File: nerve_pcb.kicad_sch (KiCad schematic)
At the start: 55 parts, among them J1 TC2050-IDC, J2 2171750001, J4 472192001, J5 BF030-16A-B1-0360-0277-0600-LB, J6 BF080-20-A-1-L-C, J7 UART, SW1 SPST, SW2 SPST, U1 ld39150dt33-r, U2 STM32F446RET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

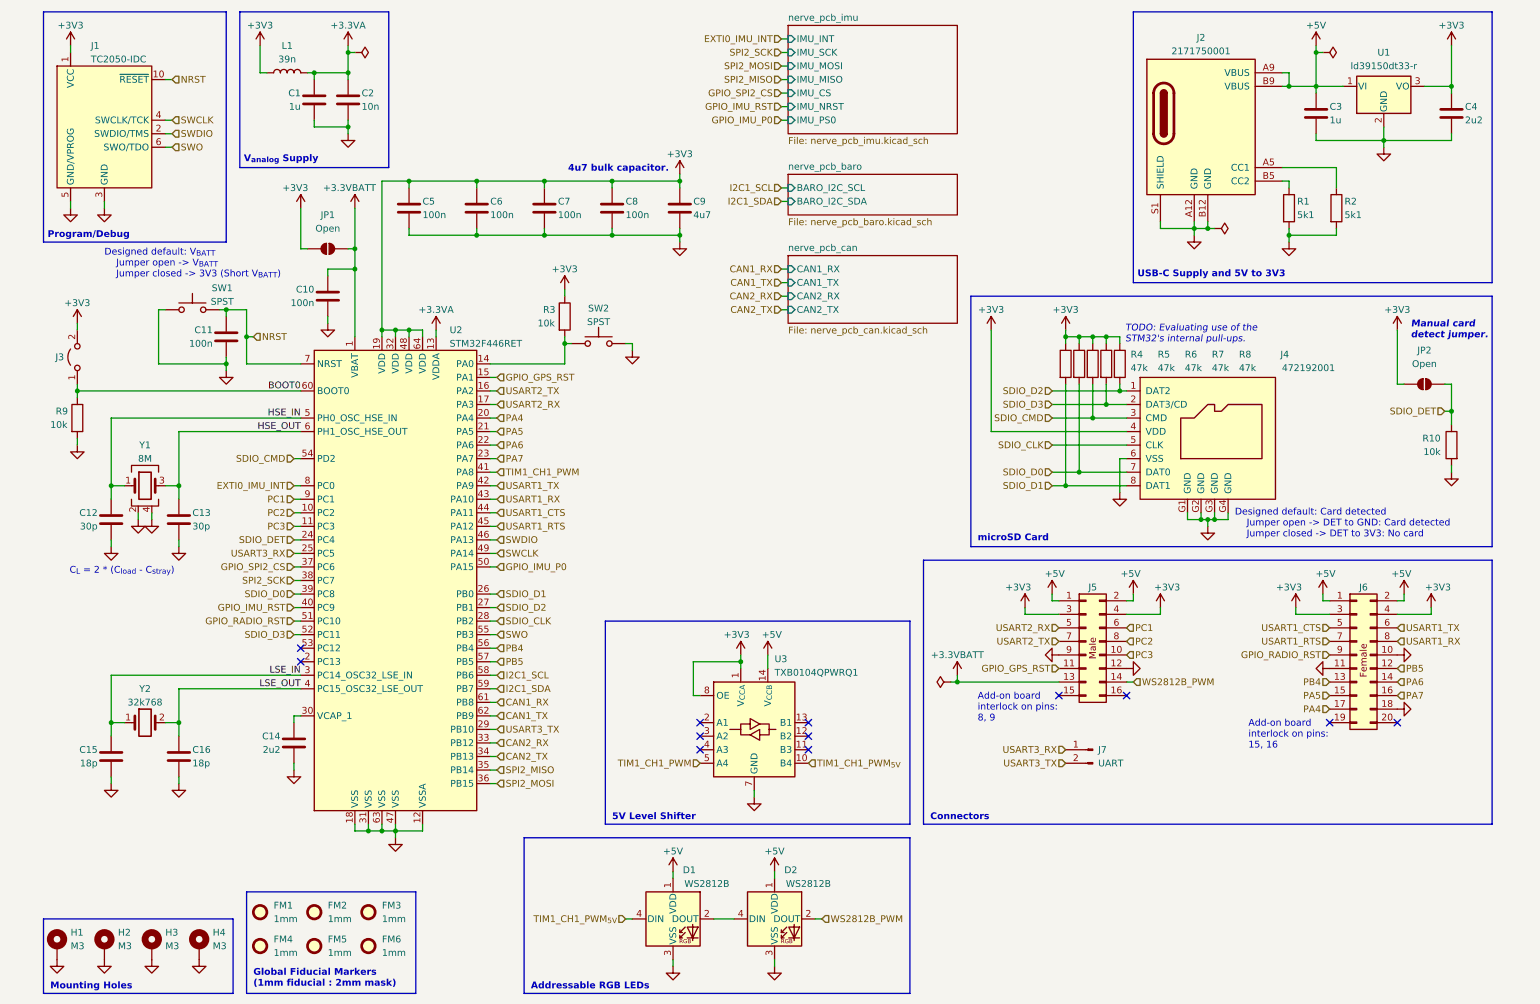
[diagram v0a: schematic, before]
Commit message: Update component_library and cleanup unused pads
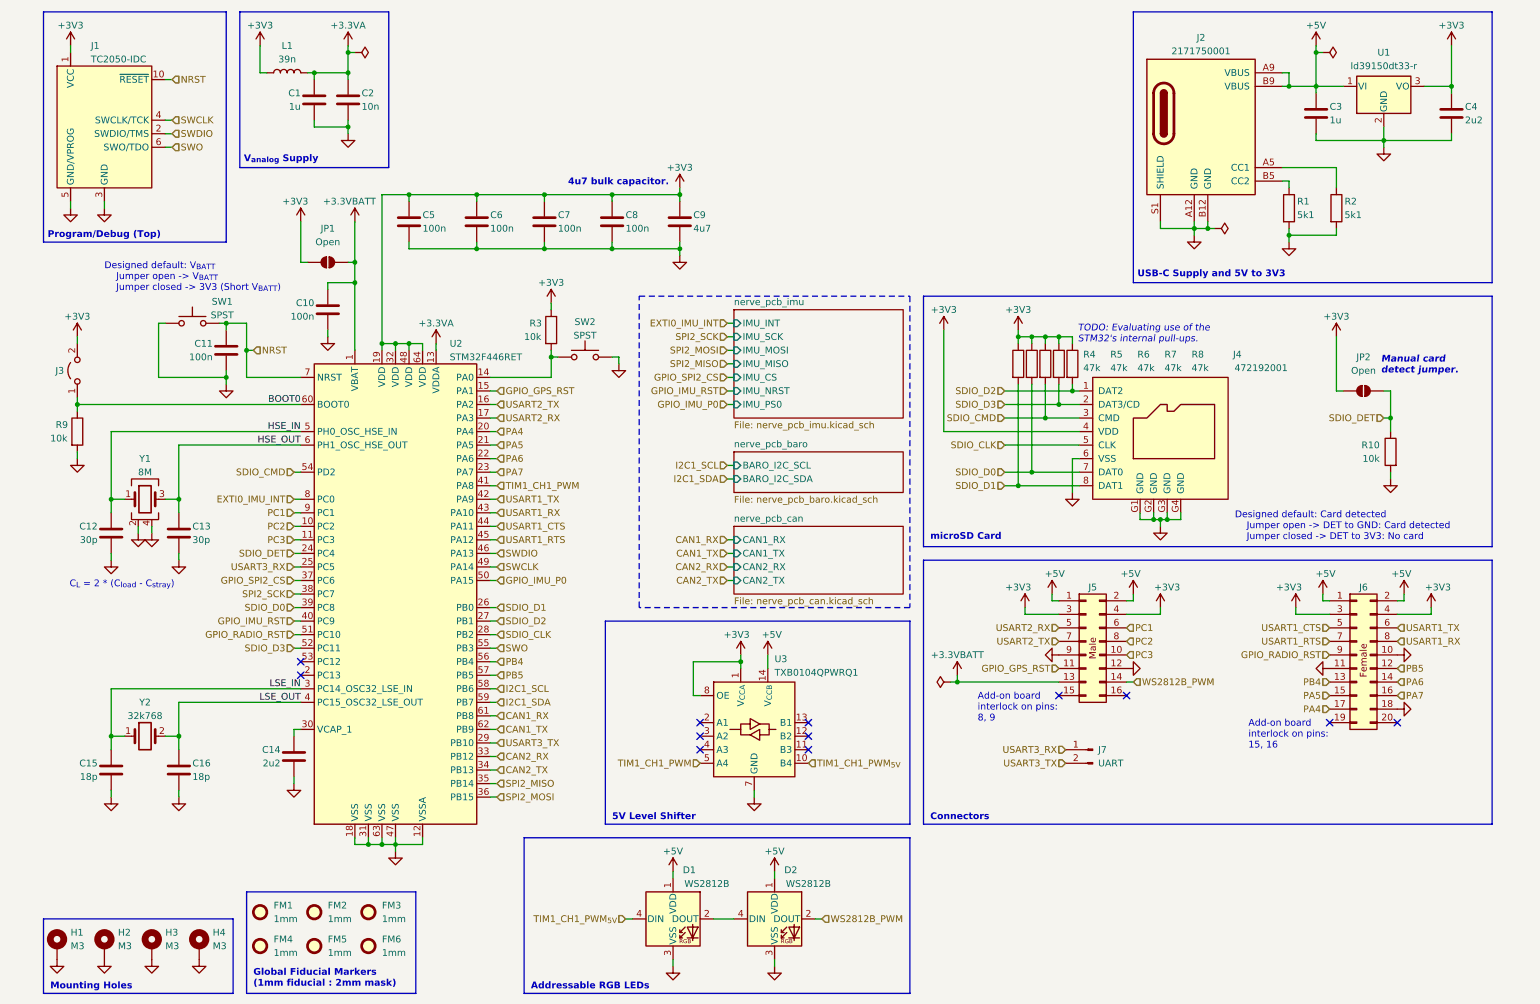
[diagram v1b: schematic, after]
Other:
- note added: "Program/Debug (Top)"
- note removed: "Program/Debug"
- moved on the sheet: C10, C11, C12, C13, C14, C15, C16, C5, C6, C7, C8, C9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

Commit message: Fix schematic notes
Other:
- note added: "4u7 bulk capacitor"
- note added: "Add-on board interlock on pins: 19, 20"
- note added: "Manual card detect jumper"
- note added: "Using external pull-ups"
- note removed: "4u7 bulk capacitor."
- note removed: "Add-on board interlock on pins: 8, 9"
- note removed: "Manual card detect jumper."
- note removed: "TODO: Evaluating use of the STM32's internal pull-ups."
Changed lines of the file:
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@@
 		)
 	)
-	(text "Add-on board\ninterlock on pins:\n8, 9"
+	(text "Add-on board\ninterlock on pins:\n15, 16"
 		(exclude_from_sim no)
 		(at 187.96 143.256 0)
@@
 		)
 	)
-	(text "Add-on board\ninterlock on pins:\n15, 16"
+	(text "Add-on board\ninterlock on pins:\n19, 20"
 		(exclude_from_sim no)
 		(at 238.76 148.336 0)
@@
 		)
 	)
-	(text "Manual card \ndetect jumper."
+	(text "Manual card \ndetect jumper"
 		(exclude_from_sim no)
 		(at 263.652 78.994 0)
@@
 		)
 	)
-	(text "4u7 bulk capacitor."
+	(text "4u7 bulk capacitor"
 		(exclude_from_sim no)
 		(at 130.048 44.704 0)
@@
 		)
 	)
-	(text "TODO: Evaluating use of the \nSTM32's internal pull-ups."
+	(text "Using external pull-ups"
 		(exclude_from_sim no)
-		(at 206.756 73.152 0)
+		(at 208.026 74.168 0)
 		(effects
 			(font
 				(size 1.27 1.27)
-				(thickness 0.1588)
+				(thickness 0.254)
+				(bold yes)
 				(italic yes)
 			)

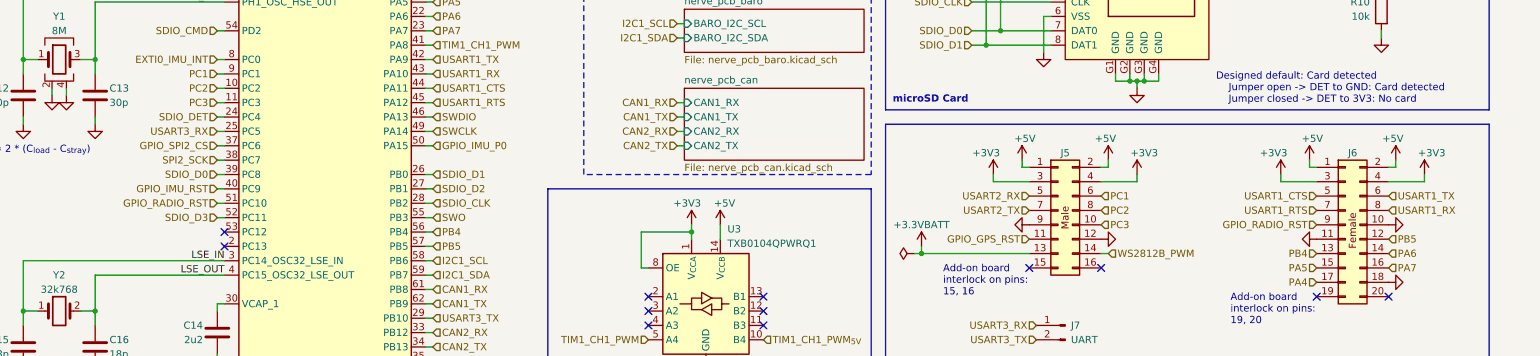
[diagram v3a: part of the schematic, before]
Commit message: Major cleanup and add missing transfer vias
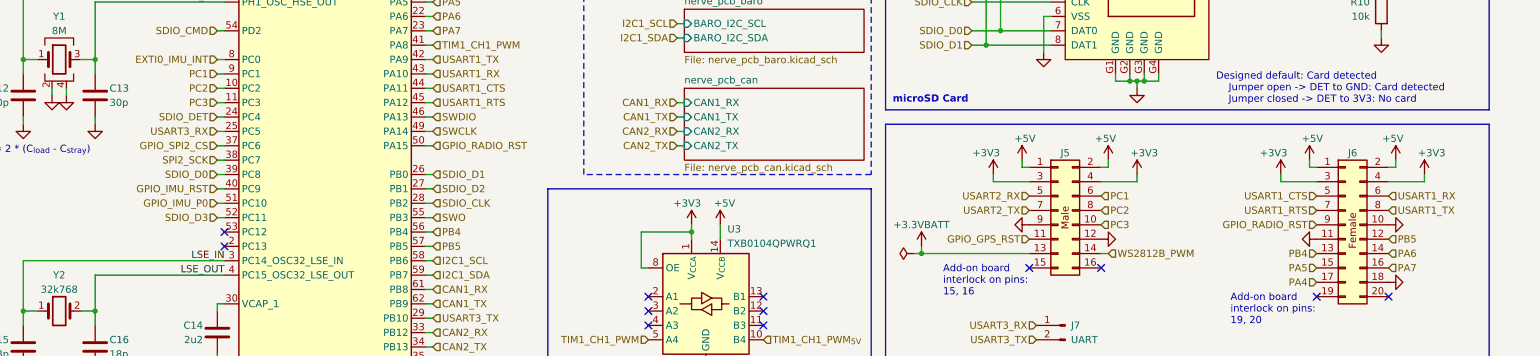
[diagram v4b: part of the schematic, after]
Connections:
- net GPIO_IMU_P0: now also U2.51 (PC10); no longer U2.50 (PA15)
- net GPIO_RADIO_RST: now also U2.50 (PA15); no longer U2.51 (PC10)
- net USART1_RX: now also J6.6; no longer J6.8
- net USART1_TX: now also J6.8; no longer J6.6

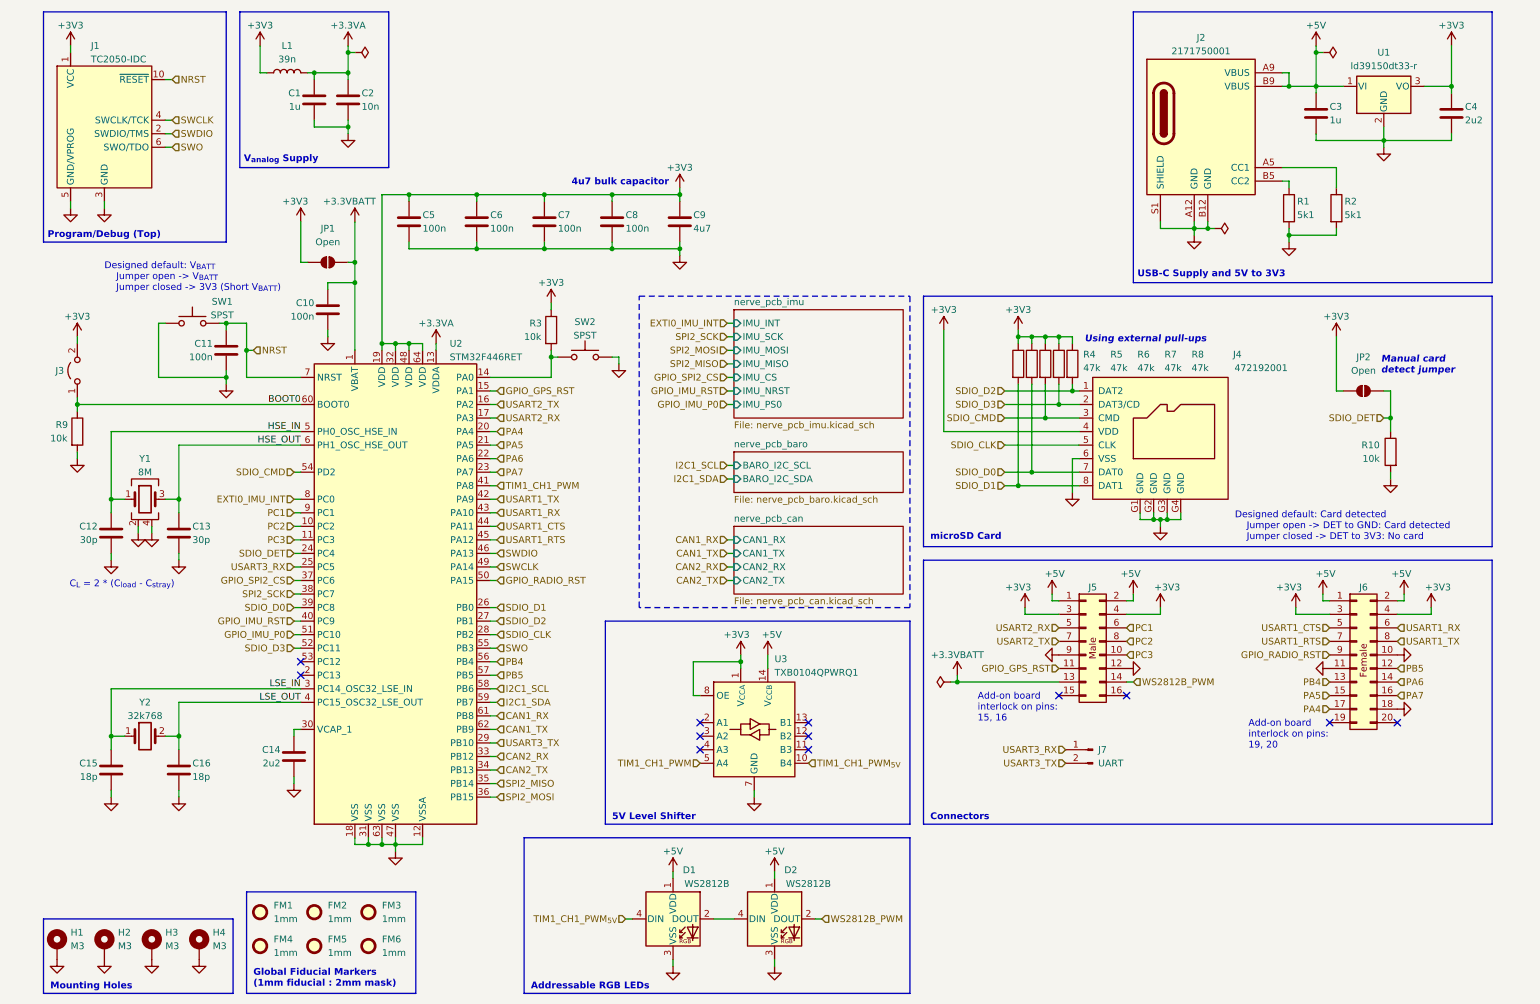
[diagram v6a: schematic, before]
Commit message: Add minor decoupling caps
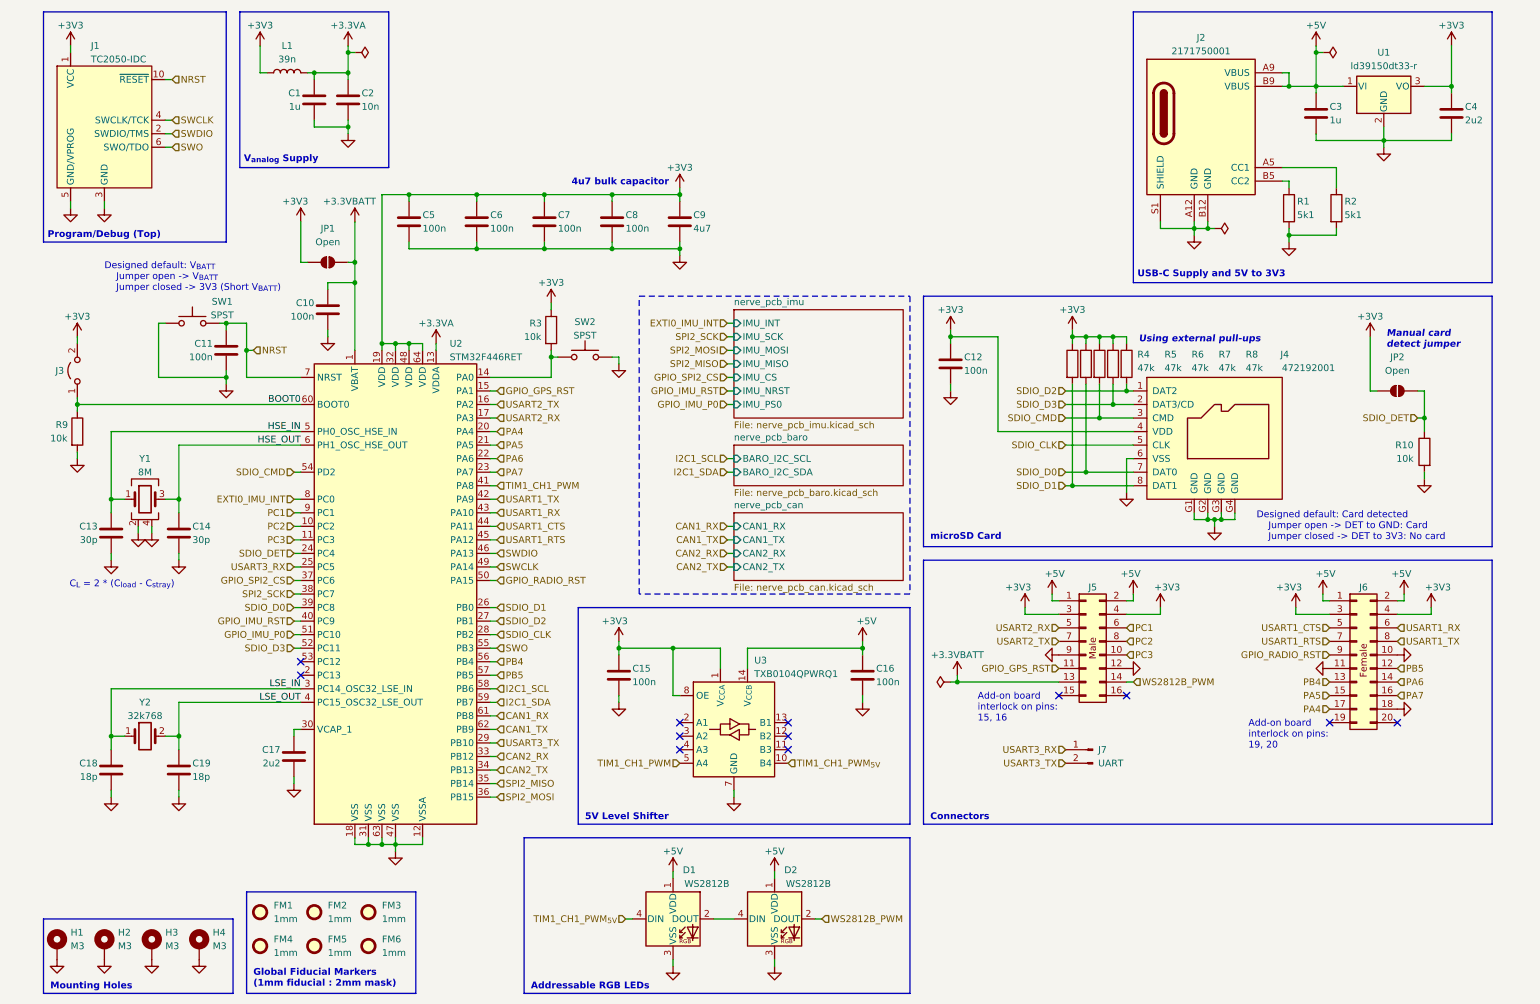
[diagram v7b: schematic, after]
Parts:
- added C12, C15, C16: 100n, Capacitor_SMD:C_0603_1608Metric, symbol Device:C
- renumbered C12 to C13, C13 to C14, C14 to C17, C15 to C18, C16 to C19
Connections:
- net +3V3: now also C12.1, C15.1
- net +5V: now also C16.1
- net GND: now also C12.2, C15.2, C16.2
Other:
- note added: "Designed default: Card detected Jumper open -> DET to GND: Card Jumper closed -> DET to 3V3: No card"
- note removed: "Designed default: Card detected Jumper open -> DET to GND: Card detected Jumper closed -> DET to 3V3: No card"
- moved on the sheet: J4, JP2, R10, R4, R5, R6, R7, R8, U3

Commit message: Update component library and pictures
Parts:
- U2: Manufacturer Part Number STM32F446RE -> STM32F446RET6
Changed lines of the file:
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@@
 			)
 		)
-		(property "Manufacturer Part Number" "STM32F446RE"
+		(property "Manufacturer Part Number" "STM32F446RET6"
 			(at 78.74 121.92 0)
 			(effects
